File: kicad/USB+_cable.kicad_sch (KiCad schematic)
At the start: 6 parts, among them J1401 USB_C_Receptacle, J1402 USB_C_Receptacle, J1403 USB3.1_full_cable

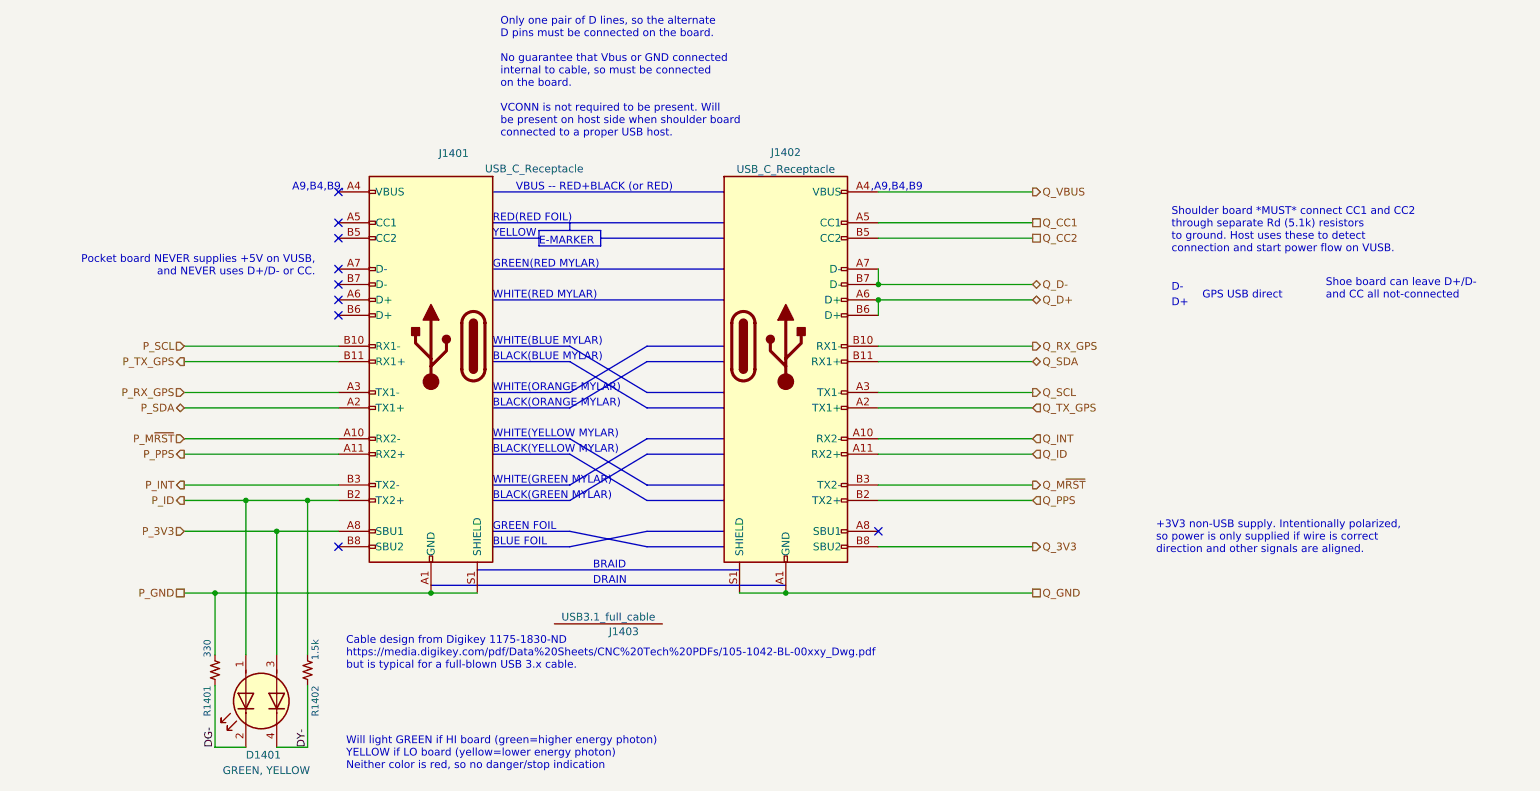
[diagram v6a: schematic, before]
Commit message: Numbering change
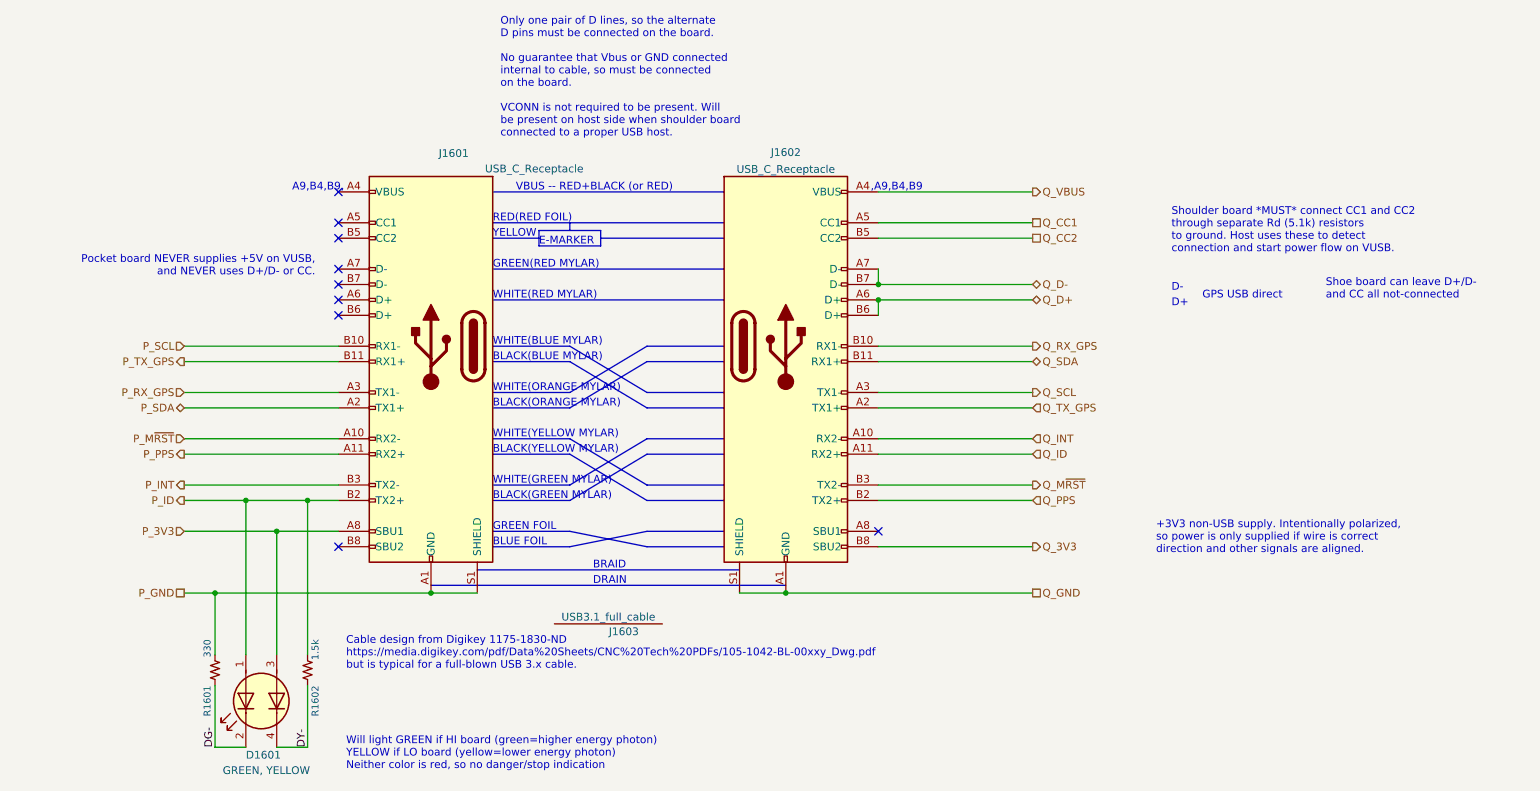
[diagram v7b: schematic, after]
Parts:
- renumbered D1401 to D1601, J1401 to J1601, J1402 to J1602, J1403 to J1603, R1401 to R1601, R1402 to R1602
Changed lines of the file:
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@@
   (symbol (lib_id "Connector:USB_C_Receptacle") (at 154.94 88.9 0) (mirror y)
     (in_bom yes) (on_board yes)
-    (property "Reference" "J1401" (id 0) (at 156.21 57.15 0)
+    (property "Reference" "J1601" (id 0) (at 156.21 57.15 0)
       (effects (font (size 1.27 1.27)) (justify right))
     )
@@
   (symbol (lib_id "Device:LED_Dual_AKAK") (at 127 147.32 90) (mirror x)
     (in_bom yes) (on_board yes)
-    (property "Reference" "D1401" (id 0) (at 124.46 156.21 90)
+    (property "Reference" "D1601" (id 0) (at 124.46 156.21 90)
       (effects (font (size 1.27 1.27)) (justify right))
     )
@@
   (symbol (lib_id "KwanSystems:RESISTOR") (at 119.38 142.24 90)
     (in_bom yes) (on_board yes)
-    (property "Reference" "R1401" (id 0) (at 118.11 144.78 0)
+    (property "Reference" "R1601" (id 0) (at 118.11 144.78 0)
       (effects (font (size 1.143 1.143)) (justify right))
     )
@@
   (symbol (lib_id "Connector:USB_C_Receptacle") (at 213.36 88.9 0)
     (in_bom yes) (on_board yes) (fields_autoplaced)
-    (property "Reference" "J1402" (id 0) (at 213.36 56.9935 0))
+    (property "Reference" "J1602" (id 0) (at 213.36 56.9935 0))
     (property "Value" "USB_C_Receptacle" (id 1) (at 213.36 59.7686 0))
     (property "Footprint" "KwanSystems:USB_C_Amphenol_MidMount" (id 2) (at 217.17 88.9 0)
@@
   (symbol (lib_id "KwanSystems:USB3.1_full_cable") (at 184.15 133.35 0)
     (in_bom yes) (on_board no)
-    (property "Reference" "J1403" (id 0) (at 186.69 135.89 0))
+    (property "Reference" "J1603" (id 0) (at 186.69 135.89 0))
     (property "Value" "USB3.1_full_cable" (id 1) (at 184.15 133.4794 0))
     (property "Footprint" "" (id 2) (at 184.15 133.35 0)
@@
   (symbol (lib_id "KwanSystems:RESISTOR") (at 134.62 142.24 90)
     (in_bom yes) (on_board yes)
-    (property "Reference" "R1402" (id 0) (at 135.89 144.78 0)
+    (property "Reference" "R1602" (id 0) (at 135.89 144.78 0)
       (effects (font (size 1.143 1.143)) (justify right))
     )
